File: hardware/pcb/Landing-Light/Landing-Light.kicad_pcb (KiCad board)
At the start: 2 copper layers, 63.5 x 21 mm, 51 parts, among them J2 Conn_01x02, J3 USB_C_Receptacle_USB2.0_16P, Q1 NMOS, Q3 NMOS, Q4 PMOS, SW1 ON_OFF, SW2 LED_COL, U1 BQ25172DSGR, U2 SRV05-4, U3 TPS61200DRC

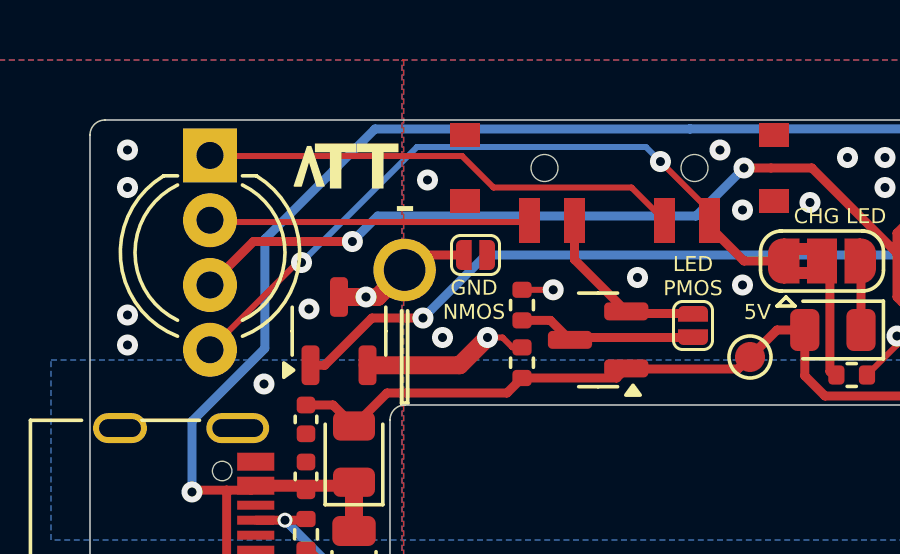
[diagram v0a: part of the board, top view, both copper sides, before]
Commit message: Route UVLO to VAUX
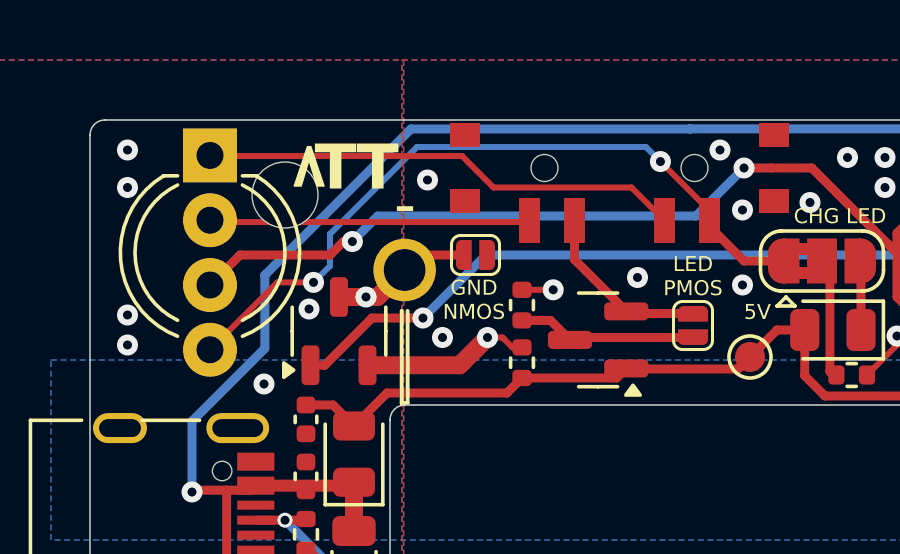
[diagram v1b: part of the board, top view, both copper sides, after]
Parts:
- added H2: MountingHole, MountingHole:MountingHole_2.2mm_M2, F.Cu at (125.0, 89.5)
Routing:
- net VIN: track 93.9 -> 93.2 mm
- net /R: track 23.8 -> 24.4 mm

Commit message: v1.3 Production
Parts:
- removed the H2 at (125.0, 89.5)
- removed JP5: SolderJumper_2_Open, Landing-Light:SolderJumper-2_P1.3mm_Open_RoundedPad0.5x0.75mm
- removed Q3: NMOS, Landing-Light:SOT-23-3-JLCPCB
- removed R3: 470k, Resistor_SMD:R_0402_1005Metric
- removed R4: 150k, Resistor_SMD:R_0402_1005Metric
- removed TP4: -BATT, TestPoint:TestPoint_Pad_D1.0mm
- added H3: MountingHole, MountingHole:MountingHole_2.2mm_M2, F.Cu at (125.0, 89.5)
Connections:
- BT1 pad 2: -BATT -> GND
- C1 pad 1: -BATT -> GND
- C10 pad 2: -BATT -> GND
- C2 pad 1: -BATT -> GND
- C8 pad 2: -BATT -> GND
- C9 pad 1: -BATT -> GND
- J2 pad 1: -BATT -> GND
- J3 pad A1: -BATT -> GND
- J3 pad A12: -BATT -> GND
- J3 pad B1: -BATT -> GND
- J3 pad B12: -BATT -> GND
- J3 pad S1: -BATT -> GND
- R12 pad 2: -BATT -> GND
- R13 pad 2: -BATT -> GND
- R15 pad 2: -BATT -> GND
- R2 pad 2: -BATT -> GND
- R5 pad 2: -BATT -> GND
- R6 pad 2: -BATT -> GND
- R7 pad 2: -BATT -> GND
- U1 pad 4: -BATT -> GND
- U1 pad 9: -BATT -> GND
- U2 pad 2: -BATT -> GND
- U3 pad 7: /UVLO -> VAUX
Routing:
- net -BATT: track 35.2 -> 0.00 mm, vias 15 -> 0
- net VAUX: track 26.4 -> 9.84 mm
- net GND: track 8.87 -> 18.9 mm, vias 30 -> 57
- net /UVLO: track 7.98 -> 0.00 mm
- net /G: track 16.0 -> 17.4 mm
- net /R: track 24.4 -> 25.7 mm, vias 2 -> 0
- net +3V3: track 37.0 -> 35.9 mm
- net /B: track 10.7 -> 11.8 mm
- removed copper zone on B.Cu, net -BATT
- removed copper zone on F.Cu, net -BATT
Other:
- board text added: "Landing Light v1.3"
- board text removed: "B-"
- board text removed: "GND NMOS"
- board text removed: "Landing Light v1.2"
